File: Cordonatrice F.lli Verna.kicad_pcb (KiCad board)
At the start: 2 copper layers, 39 parts, among them J1 Screw_Terminal_3_P5.00mm, J10 Screw_Terminal_2_P5.00mm, J11 Screw_Terminal_2_P5.00mm, J12 Screw_Terminal_4_P5.00mm, J13 Screw_Terminal_2_P5.00mm, J14 Screw_Terminal_2_P5.00mm, J2 Screw_Terminal_3_P5.00mm, J3 Screw_Terminal_3_P5.00mm, J4 Screw_Terminal_3_P5.00mm, J5 Screw_Terminal_3_P5.00mm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

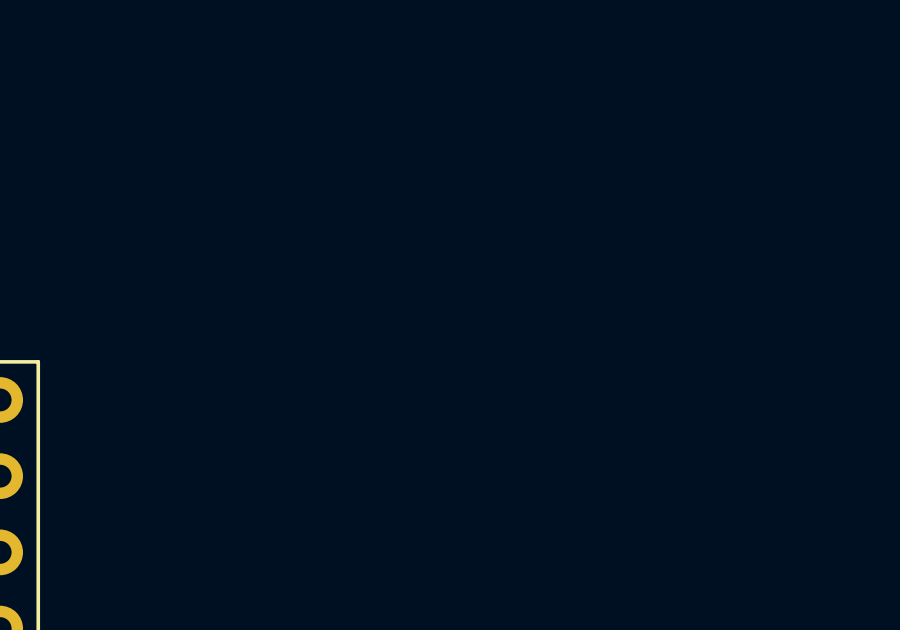
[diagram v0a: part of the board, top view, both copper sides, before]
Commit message: aggiunta diodo su transistor
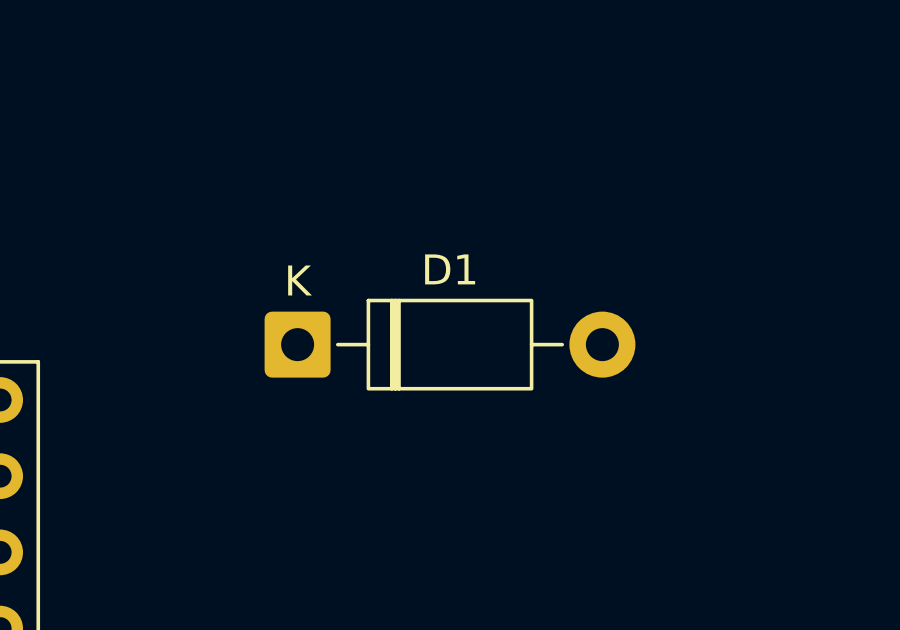
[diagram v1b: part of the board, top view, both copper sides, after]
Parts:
- added D1: 1N4007, Diode_THT:D_DO-41_SOD81_P10.16mm_Horizontal, F.Cu at (151.8, 91.5)

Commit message: applicato freerouting
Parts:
- added ForoAltoDX: MountingHole_3.5mm, MountingHole:MountingHole_3.5mm, F.Cu at (115.5, 25.0)
- added ForoAltoSX: MountingHole_3.5mm, MountingHole:MountingHole_3.5mm, F.Cu at (25.5, 25.0)
- added ForoBassoDX: MountingHole_3.5mm, MountingHole:MountingHole_3.5mm, F.Cu at (115.5, 125.0)
- added ForoBassoSX: MountingHole_3.5mm, MountingHole:MountingHole_3.5mm, F.Cu at (25.5, 125.0)
- moved U3 149.7 mm to (73.7, 74.3)
- moved C5 121.3 mm to (36.5, 107.0), turned to 90 degrees
- moved C4 114.3 mm to (44.5, 105.0), turned to -90 degrees
- moved U8 114.1 mm to (35.7, 34.7)
- moved C6 112.6 mm to (45.5, 120.5), turned to 90 degrees
- moved R9 104.9 mm to (49.5, 34.5), turned to -90 degrees
- moved C3 104.8 mm to (52.8, 119.5)
- moved U2 104.3 mm to (41.6, 60.7)
- moved U1 101.9 mm to (50.0, 107.0)
- moved R5 101.1 mm to (49.5, 32.1), turned to 90 degrees
- moved U7 95.4 mm to (55.7, 34.7)
- moved J11 91.0 mm to (27.5, 105.5), turned to -90 degrees
- moved J10 90.9 mm to (27.5, 94.0), turned to -90 degrees
- moved J9 90.8 mm to (27.5, 82.5), turned to -90 degrees
- moved J13 88.5 mm to (33.0, 121.4)
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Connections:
- J5 pad 1: STEP_PIN_X -> ENABLE_PIN_X
- J5 pad 3: ENABLE_PIN_X -> STEP_PIN_X
- J6 pad 1: STEP_PIN_Y -> ENABLE_PIN_Y
- J6 pad 3: ENABLE_PIN_Y -> STEP_PIN_Y
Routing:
- net GND: track 0.00 -> 392.2 mm
- net +24V: track 0.00 -> 194.5 mm
- net +3.3V: track 0.00 -> 162.9 mm
- net +5V: track 0.00 -> 120.1 mm, vias 0 -> 1
- net BT_PAUSE: track 0.00 -> 85.3 mm, vias 0 -> 1
- net LIMIT_X_MIN: track 0.00 -> 75.8 mm, vias 0 -> 1
- net LIMIT_X_MAX: track 0.00 -> 57.4 mm, vias 0 -> 1
- net Net-(J14-Pad1): track 0.00 -> 42.2 mm
- net LIMIT_Y_MAX: track 0.00 -> 38.7 mm
- net SDA: track 0.00 -> 37.5 mm
- net Net-(J14-Pad2): track 0.00 -> 36.7 mm
- net SCL: track 0.00 -> 35.6 mm
- net BT_STOP: track 0.00 -> 35.1 mm
- net BT_START: track 0.00 -> 34.5 mm
- net Net-(U1-VO): track 0.00 -> 34.0 mm
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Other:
- board outline added: 98 x 108 mm

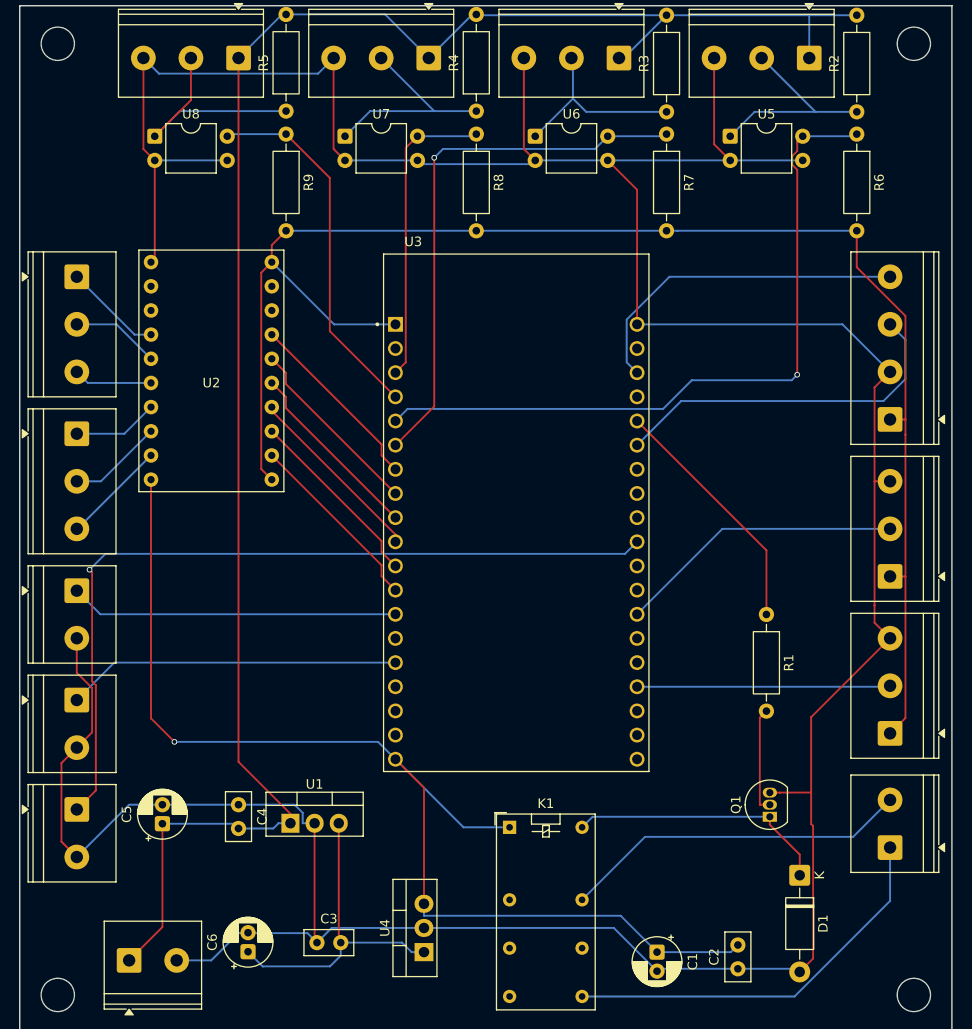
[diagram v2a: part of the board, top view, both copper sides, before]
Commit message: secondo aggiornamento piste
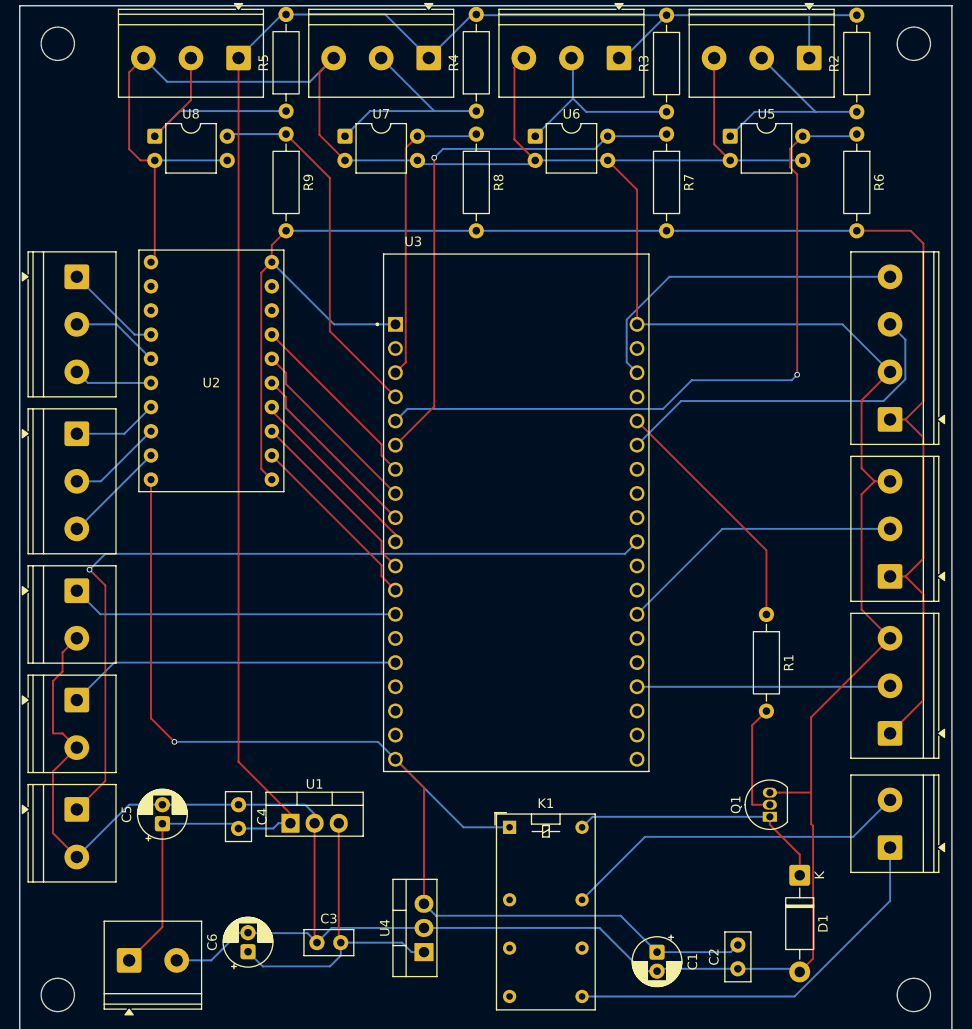
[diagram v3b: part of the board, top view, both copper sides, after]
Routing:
- net GND: track 392.2 -> 401.3 mm
- net +3.3V: track 162.9 -> 170.9 mm
- net Net-(Q1-B): track 11.2 -> 12.3 mm
- net +5V: track 120.1 -> 119.4 mm
- net BT_PAUSE: track 85.3 -> 85.9 mm
